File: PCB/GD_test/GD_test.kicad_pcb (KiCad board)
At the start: 2 copper layers, 46 x 51.3 mm, 47 parts, among them J1 RF_IN, J2 RF_IN, J3 RF_IN, J4 RF_IN, J5 Conn_01x01_Pin, J6 Conn_01x01_Pin, Q1 EPC2051, Q2 EPC2051, Q3 EPC2070, Q5 EPC2014C, U1 LMG1020YFF, U10 TLV3501, U11 LMG1020YFF, U2 TLV3501, U3 NC7WZ04, U4 TLV3501, U5 NC7WZ04, U6 NC7WZ04, U7 NC7WZ04, U8 TLV3501, U9 LMG1020YFF

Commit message: gate driver gerbers and some extra changes
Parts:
- C1, C10, C15, C16, C2, C3, C4: footprint Resistor_SMD:R_0603_1608Metric_Pad0.98x0.95mm_HandSolder -> Capacitor_SMD:C_0603_1608Metric_Pad1.08x0.95mm_HandSolder
- C12, C14: footprint Resistor_SMD:R_0402_1005Metric_Pad0.72x0.64mm_HandSolder -> Capacitor_SMD:C_0603_1608Metric_Pad1.08x0.95mm_HandSolder
- C17, C7, C8, C9: footprint Resistor_SMD:R_0603_1608Metric_Pad0.98x0.95mm_HandSolder -> Capacitor_SMD:C_0402_1005Metric_Pad0.74x0.62mm_HandSolder
- C6: footprint Resistor_SMD:R_0402_1005Metric_Pad0.72x0.64mm_HandSolder -> Capacitor_SMD:C_0402_1005Metric_Pad0.74x0.62mm_HandSolder
- moved Q1 3.40 mm to (140.3, 76.9)
- moved C9 2.97 mm to (137.8, 72.8)
- moved C17 2.77 mm to (137.9, 81.3), turned to 180 degrees
- moved U5 2.64 mm to (137.9, 74.6)
- moved U7 2.61 mm to (137.9, 79.6)
- moved U6 2.58 mm to (137.9, 77.1)
- moved C7 1.90 mm to (135.4, 79.0), turned to 180 degrees
- moved U3 1.19 mm to (135.4, 77.1)
- moved C8 1.07 mm to (135.4, 75.3), turned to 180 degrees
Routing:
- net +5V: track 192.4 -> 186.2 mm, vias 0 -> 5
- net GND: track 2.77 -> 4.52 mm, vias 335 -> 341
- net /BUFF_OUT+: track 9.44 -> 8.25 mm, vias 0 -> 2
- net /BUFF_OUT-: track 9.45 -> 8.34 mm, vias 2 -> 4
- net Net-(Q1-G): track 10.4 -> 9.54 mm
- net Net-(U3-A1): track 2.56 -> 1.90 mm
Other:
- board text added: "GaN Driver Test Board"
- board text added: "calvinlin@stanford.edu"

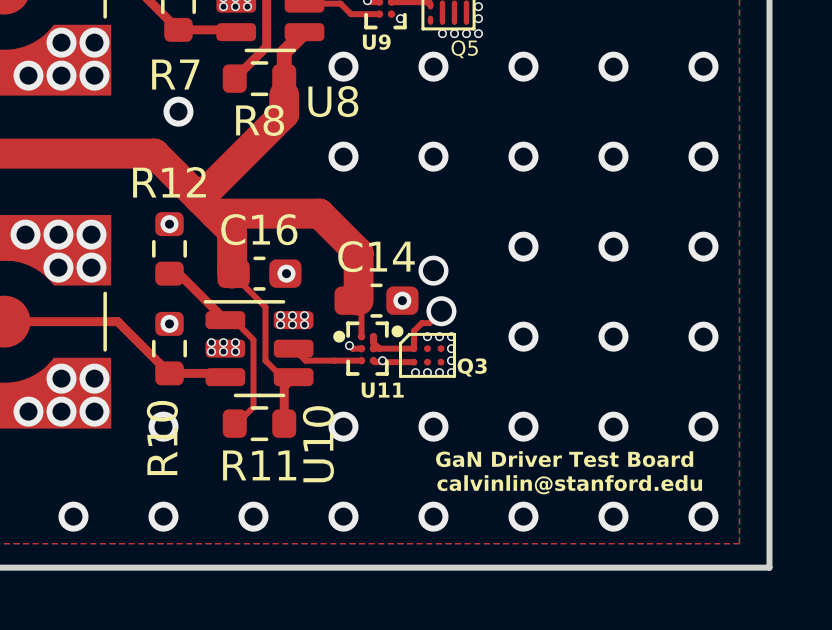
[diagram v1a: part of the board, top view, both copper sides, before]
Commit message: gate driver test board changes
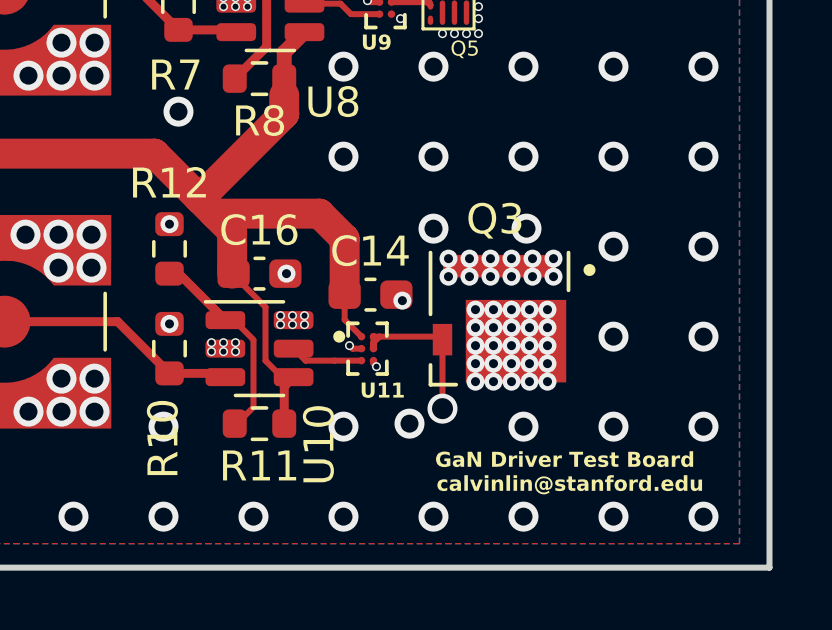
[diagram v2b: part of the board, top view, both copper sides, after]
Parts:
- Q3: value EPC2070 -> GS61004B-MR; footprint EPCGaN:BGA-6_3x2_6.0x6.0mm -> EPCGaN:TRANS_GS61004B-MR
- moved Q3 2.69 mm to (140.0, 108.5)
- moved C14 0.28 mm to (135.7, 107.7)
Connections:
- Q3 pad 1: Net-(Q3-G) -> GND
- Q3 pad 2: GND -> Net-(U11-OUTH)
- U11 pad A2: Net-(Q3-G) -> Net-(U11-OUTH)
- U11 pad B2: Net-(Q3-G) -> Net-(U11-OUTH)
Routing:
- net Net-(U11-OUTH): track 0.00 -> 5.52 mm, vias 0 -> 1
- net Net-(Q3-G): track 4.01 -> 0.00 mm, vias 1 -> 0
- net GND: track 4.52 -> 3.39 mm, vias 341 -> 368

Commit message: gate driver testboard rev 3 stuff
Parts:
- removed Q1: EPC2051, EPCGaN:BGA-6_3x2_6.0x6.0mm
- removed U3, U5, U6, U7: NC7WZ04, pcbparts:SOIC-6
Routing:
- net Net-(Q1-G): track 9.54 -> 0.00 mm
- net +5V: track 186.2 -> 177.6 mm, vias 5 -> 3
- net /BUFF_OUT-: track 8.34 -> 0.00 mm, vias 4 -> 0
- net /BUFF_OUT+: track 8.25 -> 0.00 mm, vias 2 -> 0
- net GND: track 3.39 -> 1.47 mm, vias 368 -> 350

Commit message: gate driver test board rev 2 gerbers commit
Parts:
- removed C3: C_Small, Capacitor_SMD:C_0603_1608Metric_Pad1.08x0.95mm_HandSolder
- removed Q5: EPC2014C, EPCGaN:EPC2014C
- added C11: C_Small, Capacitor_SMD:C_0402_1005Metric, F.Cu at (139.0, 81.6)
- added C13: C_Small, Capacitor_SMD:C_0402_1005Metric, F.Cu at (135.8, 96.2)
- added C18: C_Small, Capacitor_SMD:CP_Elec_10x10, F.Cu at (109.4, 87.4)
- added C5: C_Small, Capacitor_SMD:C_0603_1608Metric, F.Cu at (132.4, 95.6)
- added Q1: GS61004B-MR, EPCGaN:TRANS_GS61004B-MR, F.Cu at (145.4, 76.5)
- added Q4: EPC2214, pcbparts:BGA-9_3x3_6.0x6.0mm, F.Cu at (142.5, 97.8)
- added R13: 1, Resistor_SMD:R_0402_1005Metric, F.Cu at (137.2, 109.2)
- added R14: 1, Resistor_SMD:R_0402_1005Metric, F.Cu at (142.2, 77.0)
- added U12: NC7WZ04, pcbparts:nc7wz04_sc-88_SOIC-6, F.Cu at (139.8, 95.4)
- added U13: NC7WZ04, pcbparts:nc7wz04_sc-88_SOIC-6, F.Cu at (139.8, 98.0)
- added U14: NC7WZ04, pcbparts:nc7wz04_sc-88_SOIC-6, F.Cu at (139.8, 100.6)
- added U3: NC7WZ04, pcbparts:nc7wz04_sc-88_SOIC-6, F.Cu at (136.0, 77.2)
- added U5: NC7WZ04, pcbparts:nc7wz04_sc-88_SOIC-6, F.Cu at (139.5, 74.6)
- added U6: NC7WZ04, pcbparts:nc7wz04_sc-88_SOIC-6, F.Cu at (139.5, 77.2)
- added U7: NC7WZ04, pcbparts:nc7wz04_sc-88_SOIC-6, F.Cu at (139.5, 79.8)
- C1, C10, C16, C2, C4: footprint Capacitor_SMD:C_0603_1608Metric_Pad1.08x0.95mm_HandSolder -> Capacitor_SMD:C_0603_1608Metric
- C12, C14, C15: footprint Capacitor_SMD:C_0603_1608Metric_Pad1.08x0.95mm_HandSolder -> Capacitor_SMD:C_0402_1005Metric
- C17, C6, C7, C8, C9: footprint Capacitor_SMD:C_0402_1005Metric_Pad0.74x0.62mm_HandSolder -> Capacitor_SMD:C_0402_1005Metric
- Q2: value EPC2051 -> EPC2214; footprint EPCGaN:BGA-6_3x2_6.0x6.0mm -> pcbparts:BGA-9_3x3_6.0x6.0mm
- U9: value LMG1020YFF -> NC7WZ04; footprint GateDriver:BGA6N40P3X2_125X85X62N -> pcbparts:nc7wz04_sc-88_SOIC-6
- moved C7 23.9 mm to (139.2, 102.5)
- moved C15 5.52 mm to (135.9, 99.8)
- moved C8 4.20 mm to (138.9, 72.9), turned to 0 degrees
- moved C12 4.14 mm to (138.9, 93.5)
- moved J6 3.93 mm to (110.7, 99.8)
- moved J5 3.53 mm to (110.0, 75.3)
- moved C17 3.39 mm to (135.4, 79.0)
- moved C9 3.39 mm to (135.5, 75.3), turned to 0 degrees
- moved J2 0.81 mm to (124.3, 97.3)
- moved C14 0.58 mm to (135.2, 108.0)
- moved Q3 0.55 mm to (140.6, 108.5)
- moved J4 0.55 mm to (124.0, 76.5)
- moved J1 0.50 mm to (124.0, 87.2)
- moved C2 0.50 mm to (115.5, 86.9)
- moved J3 0.50 mm to (124.0, 108.6)
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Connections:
- C12 pad 1: +5V -> GND
- C12 pad 2: GND -> +5V
- C15 pad 1: +5V -> GND
- C15 pad 2: GND -> +5V
- C8 pad 1: +5V -> GND
- C8 pad 2: GND -> +5V
- C9 pad 1: +5V -> GND
- C9 pad 2: GND -> +5V
- Q3 pad 2: Net-(U11-OUTH) -> Net-(Q3-Pad2)
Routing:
- net +5V: track 177.6 -> 229.9 mm, vias 3 -> 0
- net Net-(U5-Y1): track 0.00 -> 14.3 mm
- net Net-(Q4-G): track 0.00 -> 13.8 mm, vias 0 -> 1
- net Net-(U3-Y1): track 0.00 -> 13.2 mm
- net /inv_out: track 0.00 -> 13.0 mm
- net Net-(U11-OUTH): track 5.52 -> 1.81 mm, vias 1 -> 0
- net Net-(Q5-G): track 3.70 -> 0.00 mm, vias 1 -> 0
- net Net-(Q1-Pad2): track 0.00 -> 2.36 mm, vias 0 -> 1
- net Net-(Q3-Pad2): track 0.00 -> 2.28 mm, vias 0 -> 1
- net /RF_IN_3: track 8.33 -> 7.59 mm
- net Net-(U3-A1): track 1.90 -> 2.57 mm
- net /RF_IN_2: track 7.76 -> 7.21 mm
- net Net-(U8-OUT): track 2.64 -> 2.13 mm
- net /RF_IN_4: track 8.13 -> 7.63 mm
- net GND: track 1.47 -> 1.05 mm, vias 350 -> 392
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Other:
- board size 46 x 51.3 mm -> 51.4 x 51.3 mm
- board text added: "GaN Driver Test Board Rev 2"
- board text removed: "GaN Driver Test Board"
